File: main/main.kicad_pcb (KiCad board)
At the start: 2 copper layers, 105 x 160 mm, 120 parts, among them J1 Conn_01x05, J2 Conn_02x32_Row_Letter_Last, J3 SCART-F, J4 AudioJack2_Dual_Ground_Switch, J5 DB15_Female_HighDensity_Mount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, J6 Conn_02x03_Odd_Even, Q1 MMBT3904, Q2 MMBT3904, Q3 DTC144EKA, SW1 PBSW_4PDT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

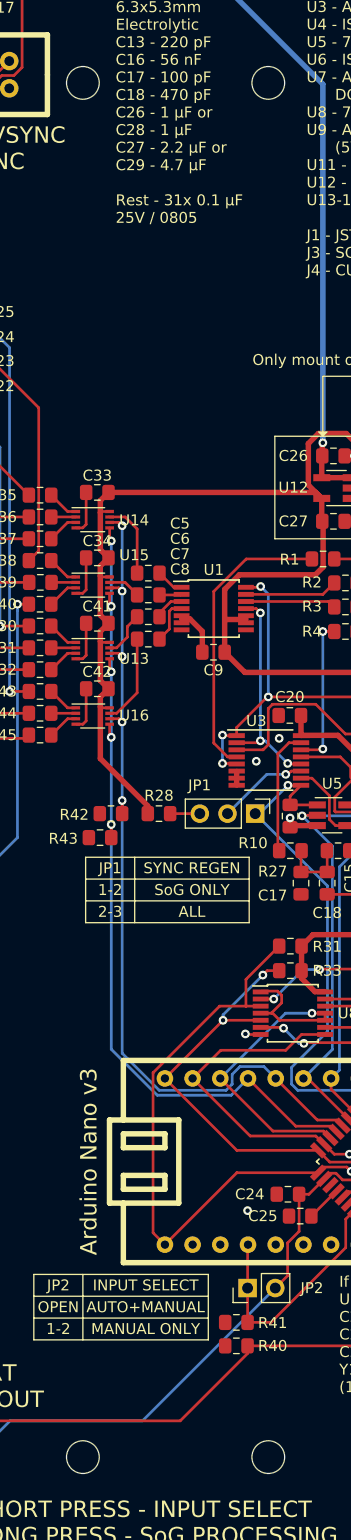
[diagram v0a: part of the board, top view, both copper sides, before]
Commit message: Use proper mounting holes rather than edge cuts
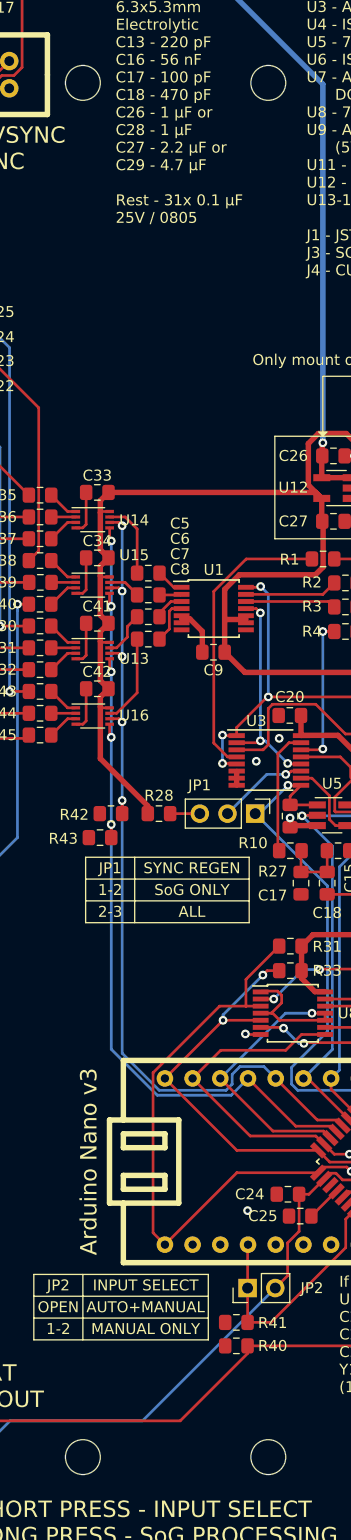
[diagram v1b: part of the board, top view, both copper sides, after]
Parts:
- added H1: MountingHole, MountingHole:MountingHole_3.2mm_M3, F.Cu at (71.0, 37.0)
- added H2: MountingHole, MountingHole:MountingHole_3.2mm_M3, F.Cu at (71.0, 163.0)
- added H3: MountingHole, MountingHole:MountingHole_3.2mm_M3, F.Cu at (88.0, 37.0)
- added H4: MountingHole, MountingHole:MountingHole_3.2mm_M3, F.Cu at (88.0, 163.0)
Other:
- outline, holes or cut-outs redrawn

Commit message: Cool kids give credit
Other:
- board text added: "Matt Dainty (github.com/bodgit/bkm-129x-ultimate)"
- board text added: "Thanks to Martin Hejnfelt for reverse engineering and creating the original BKM-129X compatible clones"
